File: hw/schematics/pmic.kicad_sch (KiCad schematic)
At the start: 40 parts, among them J1 TYPE-C-31-M-13C, J2 Conn_01x02, U2 NPM1300-QEAA-R

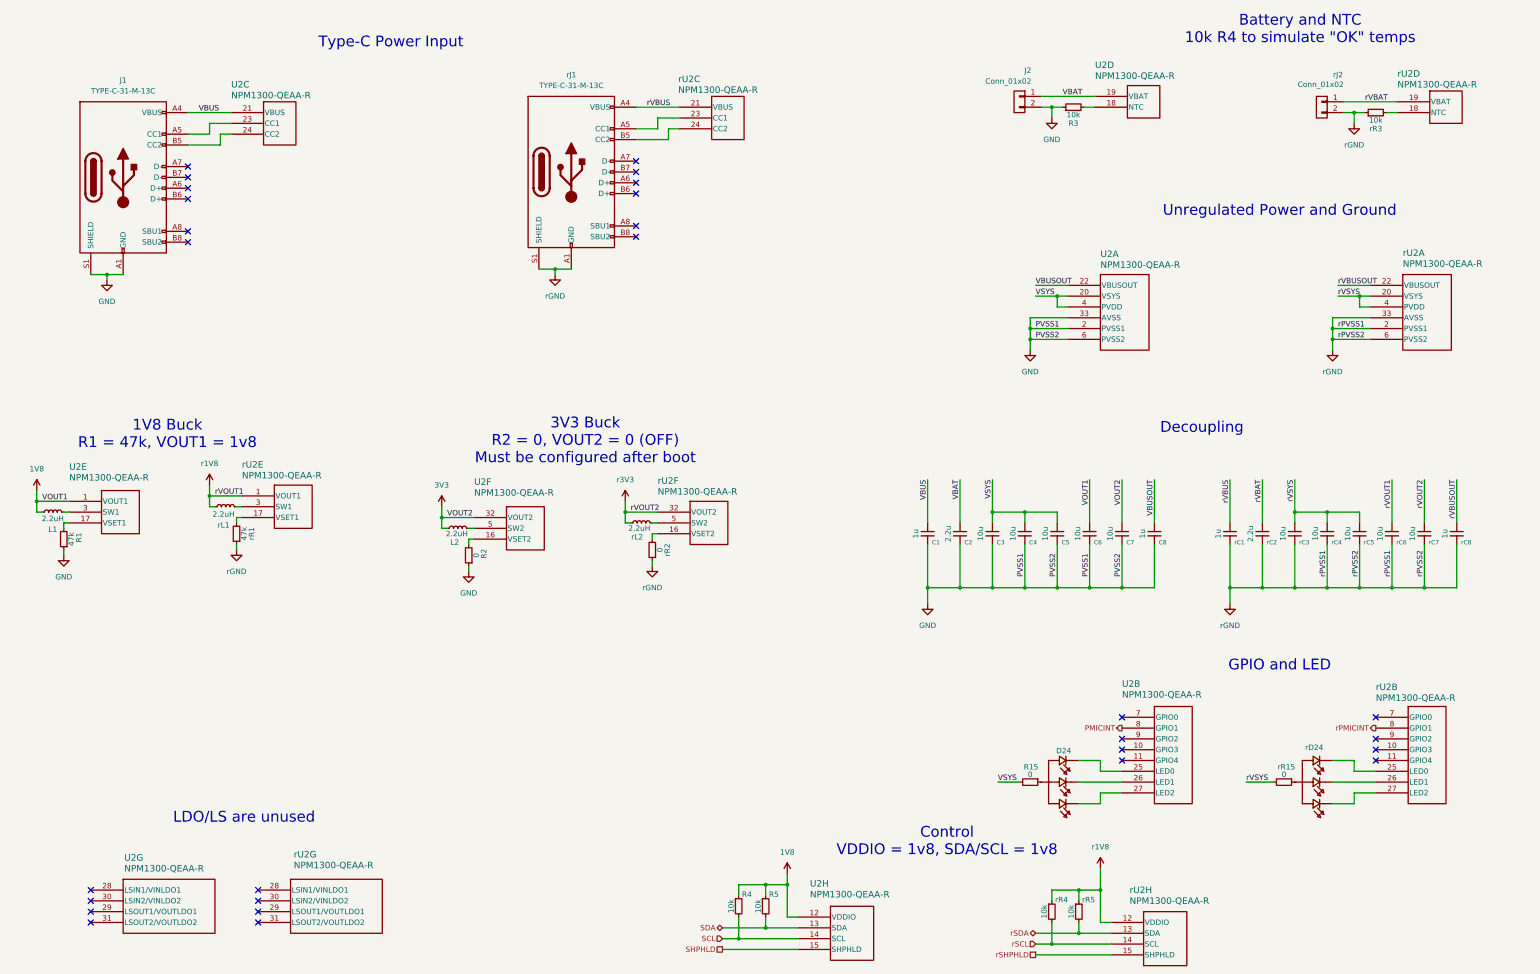
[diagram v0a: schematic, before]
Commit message: Rename power rails
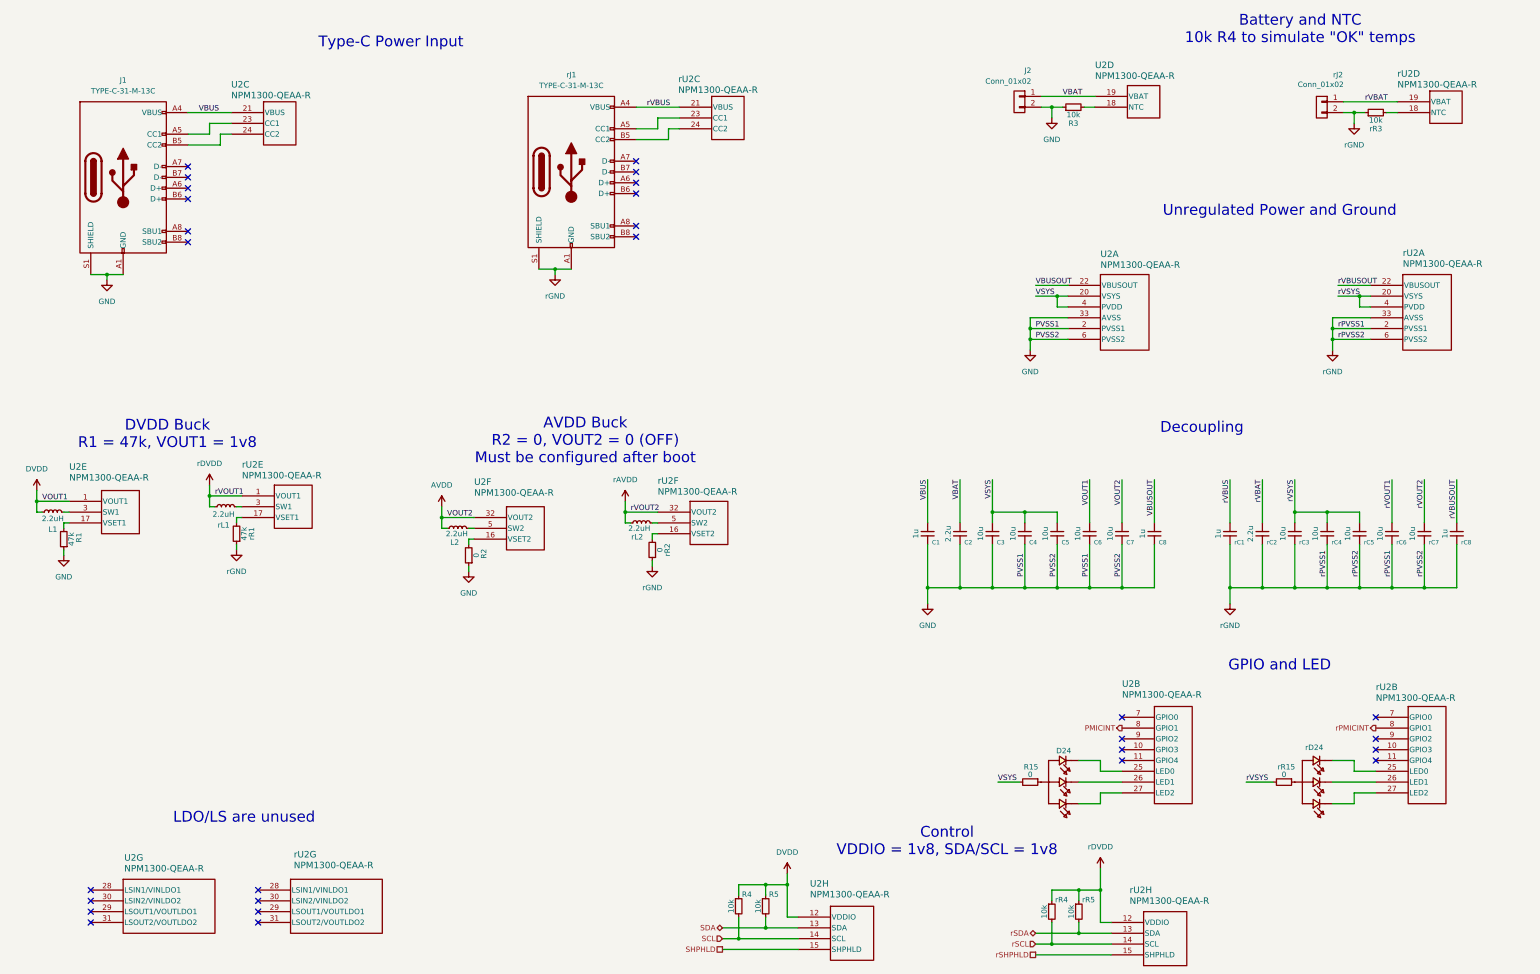
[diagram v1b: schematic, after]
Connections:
- net 1V8 renamed DVDD
- net 3V3 renamed AVDD
- net r1V8 renamed rDVDD
- net r3V3 renamed rAVDD
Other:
- note added: "AVDD Buck R2 = 0, VOUT2 = 0 (OFF) Must be configured after boot"
- note added: "DVDD Buck R1 = 47k, VOUT1 = 1v8"
- note removed: "1V8 Buck R1 = 47k, VOUT1 = 1v8"
- note removed: "3V3 Buck R2 = 0, VOUT2 = 0 (OFF) Must be configured after boot"
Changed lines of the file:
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@@
 		)
 	)
-	(text "3V3 Buck\nR2 = 0, VOUT2 = 0 (OFF)\nMust be configured after boot"
+	(text "AVDD Buck\nR2 = 0, VOUT2 = 0 (OFF)\nMust be configured after boot"
 		(exclude_from_sim no)
 		(at 169.672 126.746 0)
@@
 		)
 	)
-	(text "1V8 Buck\nR1 = 47k, VOUT1 = 1v8"
+	(text "DVDD Buck\nR1 = 47k, VOUT1 = 1v8"
 		(exclude_from_sim no)
 		(at 71.374 125.222 0)
@@
 	)
 	(symbol
-		(lib_id "Alidade:r1V8")
+		(lib_id "Alidade:rDVDD")
 		(at 290.83 227.33 0)
 		(unit 1)
@@
 		(dnp no)
 		(fields_autoplaced yes)
-		(property "Reference" "#r1V8_03"
+		(property "Reference" "#rDVDD0101"
 			(at 290.83 231.14 0)
 			(effects
@@
 			)
 		)
-		(property "Value" "r1V8"
+		(property "Value" "rDVDD"
 			(at 290.83 222.25 0)
 			(effects
@@
 			(project "alidade"
 				(path "/4cc5d416-57f5-4147-8183-e03ae6b1198a/29a12dcc-0491-44a2-8290-cbef7c573a8c"
-					(reference "#r1V8_03")
+					(reference "#rDVDD0101")
 					(unit 1)
 				)
@@
 	)
 	(symbol
-		(lib_id "Alidade:1V8")
+		(lib_id "Alidade:DVDD")
 		(at 40.64 138.43 0)
 		(unit 1)
@@
 		(dnp no)
 		(fields_autoplaced yes)
-		(property "Reference" "#1V8_01"
+		(property "Reference" "#DVDD0102"
 			(at 40.64 142.24 0)
 			(effects
@@
 			)
 		)
-		(property "Value" "1V8"
+		(property "Value" "DVDD"
 			(at 40.64 133.35 0)
 			(effects
@@
 			(project "alidade"
 				(path "/4cc5d416-57f5-4147-8183-e03ae6b1198a/29a12dcc-0491-44a2-8290-cbef7c573a8c"
-					(reference "#1V8_01")
+					(reference "#DVDD0102")
 					(unit 1)
 				)
@@
 	)
 	(symbol
-		(lib_id "Alidade:r3V3")
+		(lib_id "Alidade:rAVDD")
 		(at 179.07 140.97 0)
 		(unit 1)
@@
 		(dnp no)
 		(fields_autoplaced yes)
-		(property "Reference" "#r3V3_01"
+		(property "Reference" "#rAVDD0101"
 			(at 179.07 144.78 0)
 			(effects
@@
 			)
 		)
-		(property "Value" "r3V3"
+		(property "Value" "rAVDD"
 			(at 179.07 135.89 0)
 			(effects
@@
 			(project "alidade"
 				(path "/4cc5d416-57f5-4147-8183-e03ae6b1198a/29a12dcc-0491-44a2-8290-cbef7c573a8c"
-					(reference "#r3V3_01")
+					(reference "#rAVDD0101")
 					(unit 1)
 				)
@@
 	)
 	(symbol
-		(lib_id "Alidade:r1V8")
+		(lib_id "Alidade:rDVDD")
 		(at 81.28 137.16 0)
 		(unit 1)
@@
 		(dnp no)
 		(fields_autoplaced yes)
-		(property "Reference" "#r1V8_01"
+		(property "Reference" "#rDVDD0102"
 			(at 81.28 140.97 0)
 			(effects
@@
 			)
 		)
-		(property "Value" "r1V8"
+		(property "Value" "rDVDD"
 			(at 81.28 132.08 0)
 			(effects
@@
 			(project "alidade"
 				(path "/4cc5d416-57f5-4147-8183-e03ae6b1198a/29a12dcc-0491-44a2-8290-cbef7c573a8c"
-					(reference "#r1V8_01")
+					(reference "#rDVDD0102")
 					(unit 1)
 				)
@@
 	)
 	(symbol
-		(lib_name "1V8_1")
-		(lib_id "Alidade:1V8")
+		(lib_id "Alidade:DVDD")
 		(at 217.17 228.6 0)
 		(unit 1)
@@
 		(dnp no)
 		(fields_autoplaced yes)
-		(property "Reference" "#1V8_03"
+		(property "Reference" "#DVDD0101"
 			(at 217.17 232.41 0)
 			(effects
@@
 			)
 		)
-		(property "Value" "1V8"
+		(property "Value" "DVDD"
 			(at 217.17 223.52 0)
 			(effects
@@
 			(project "alidade"
 				(path "/4cc5d416-57f5-4147-8183-e03ae6b1198a/29a12dcc-0491-44a2-8290-cbef7c573a8c"
-					(reference "#1V8_03")
+					(reference "#DVDD0101")
 					(unit 1)
 				)
@@
 	)
 	(symbol
-		(lib_id "Alidade:3V3")
+		(lib_id "Alidade:AVDD")
 		(at 135.89 142.24 0)
 		(unit 1)
@@
 		(dnp no)
 		(fields_autoplaced yes)
-		(property "Reference" "#3V3_01"
+		(property "Reference" "#AVDD0101"
 			(at 135.89 146.05 0)
 			(effects
@@
 			)
 		)
-		(property "Value" "3V3"
+		(property "Value" "AVDD"
 			(at 135.89 137.16 0)
 			(effects
@@
 			(project "alidade"
 				(path "/4cc5d416-57f5-4147-8183-e03ae6b1198a/29a12dcc-0491-44a2-8290-cbef7c573a8c"
-					(reference "#3V3_01")
+					(reference "#AVDD0101")
 					(unit 1)
 				)

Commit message: Second mcu and reset refs
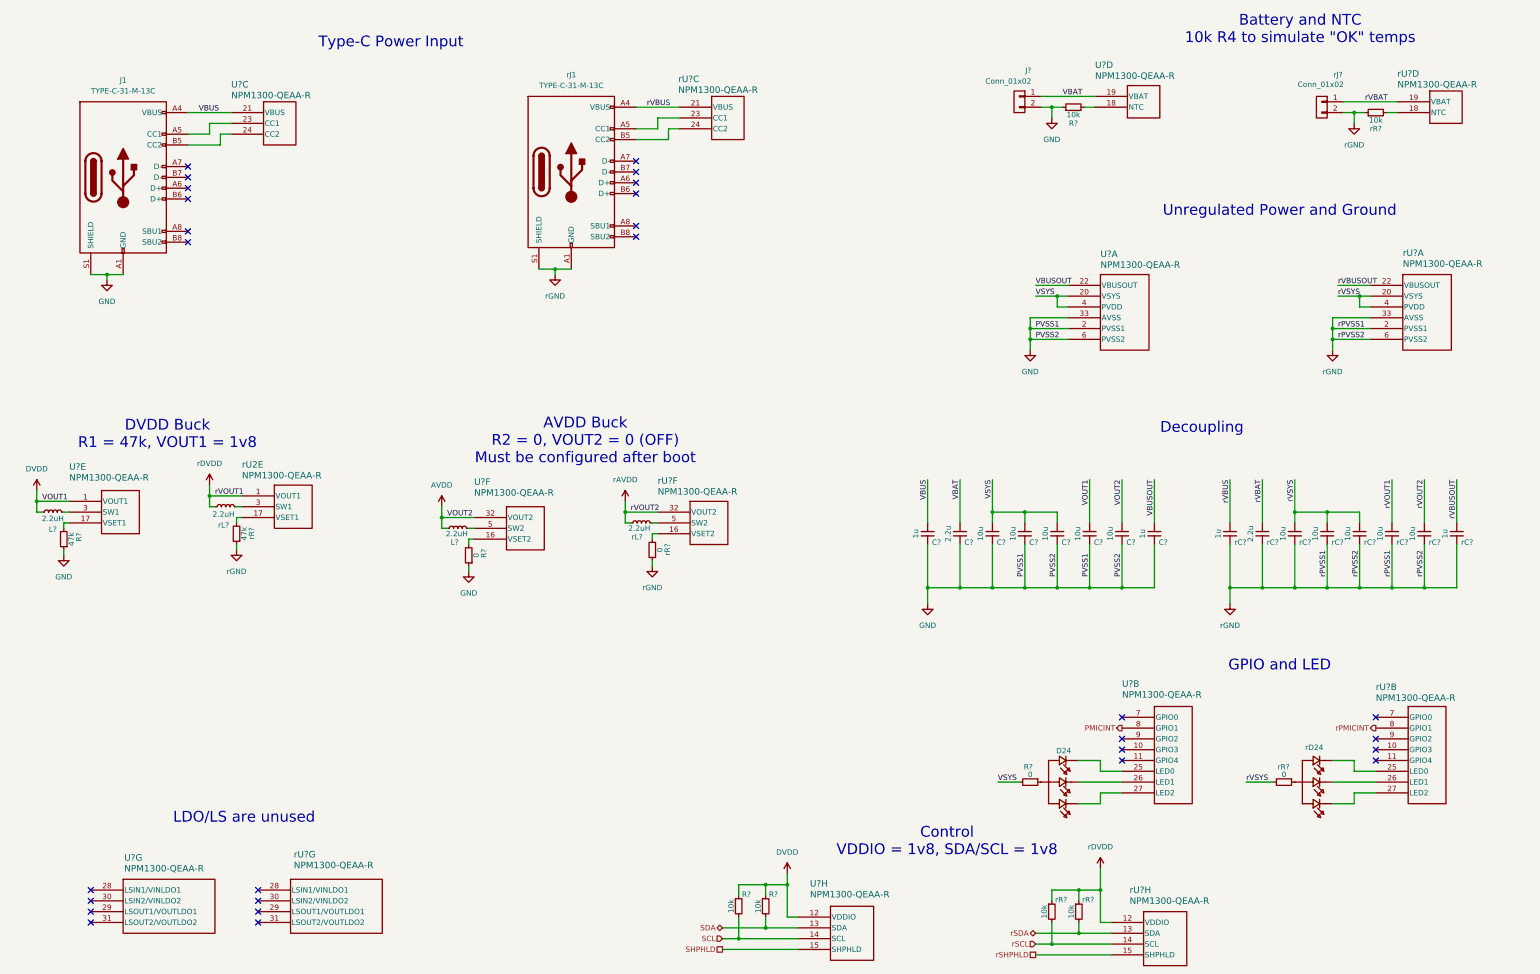
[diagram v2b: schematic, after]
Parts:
- renumbered C5 to C?, C6 to C?, C4 to C?, C3 to C?, C1 to C?, C7 to C?, C8 to C?, C2 to C?, J2 to J?, L1 to L?, L2 to L?, R5 to R?, R3 to R?, R4 to R?, R2 to R?, R1 to R?, R15 to R?, U2 to U?, rC7 to rC?, rC5 to rC?, rC6 to rC?, rC1 to rC?, rC2 to rC?, rC8 to rC?, rC3 to rC?, rC4 to rC?, rJ2 to rJ?, rL1 to rL?, rL2 to rL?, rR3 to rR?, rR1 to rR?, rR4 to rR?, rR15 to rR?, rR5 to rR?, rR2 to rR?, rU2 to rU?

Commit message: Refs and cleanup
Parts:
- removed C? (x5), rC? (x5): 10u, Alidade:0603, symbol Alidade:C
- removed C? (x2), rC? (x2): 1u, Alidade:0603, symbol Alidade:C
- removed C?, rC?: 2.2u, Alidade:0603, symbol Alidade:C
- added C1, C3, rC1, rC3: 1u, Alidade:0603, symbol Alidade:C
- added C2, rC2: 2.2u, Alidade:0603, symbol Alidade:C
- added C4, C5, C6, C7, C8, rC4, rC5, rC6, rC7, rC8: 10u, Alidade:0603, symbol Alidade:C
- gave numbers to parts that had none: 20
- renumbered rU2 to rU1
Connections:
- net AVDD: now also C8.1
- net DVDD: now also C7.1
- net GND: now also C1.2, C2.2, C3.2, C4.2, C5.2, C6.2, C7.2, C8.2
- net VSYS: now also C4.1, C5.1, C6.1
- net rAVDD: now also rC8.1
- net rDVDD: now also rC7.1
- net rGND: now also rC1.2, rC2.2, rC3.2, rC4.2, rC5.2, rC6.2, rC7.2, rC8.2
- net rVBUS: now also rC1.1
- net rVSYS: now also rC4.1, rC5.1, rC6.1
- net VBAT: no longer names the net of J2.1 (Pin_1), U1.19 (VBAT)
- net VBAT: now also C2.1
- net VBUS: no longer names the net of J1.A4 (VBUS), J1.A9 (VBUS), J1.B4 (VBUS), J1.B9 (VBUS), U1.21 (VBUS)
- net VBUS: now also C1.1
- net VBUSOUT: no longer names the net of U1.22 (VBUSOUT)
- net VBUSOUT: now also C3.1
- net rVBAT: no longer names the net of rJ2.1 (Pin_1), rU1.19 (VBAT)
- net rVBAT: now also rC2.1
- net rVBUSOUT: no longer names the net of rU1.22 (VBUSOUT)
- net rVBUSOUT: now also rC3.1
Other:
- note removed: "Decoupling"
- moved on the sheet: D24, J2, L1, L2, R1, R4, R5, R6, U1A, U1B, U1D, U1H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
